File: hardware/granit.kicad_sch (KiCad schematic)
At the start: 8 parts

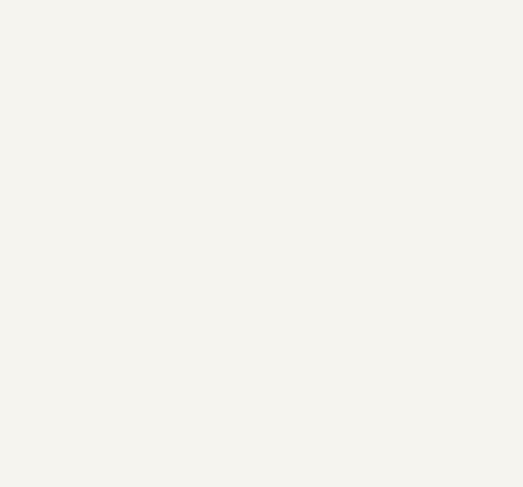
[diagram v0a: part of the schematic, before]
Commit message: feat: add OSHW logo (SYM1) to schematic and PCB
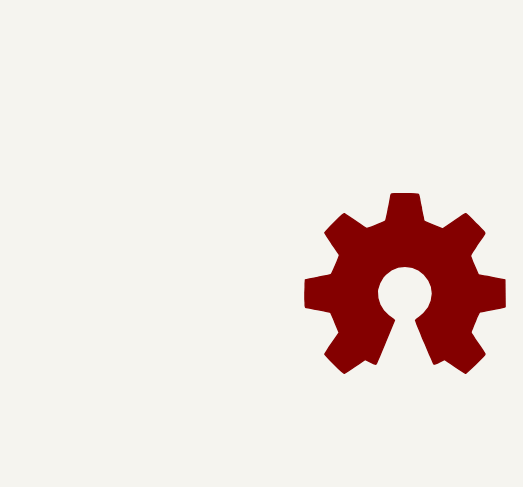
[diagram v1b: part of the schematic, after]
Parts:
- added SYM1: Logo_Open_Hardware_Large, Symbol:OSHW-Logo2_7.3x6mm_SilkScreen, symbol Graphic:Logo_Open_Hardware_Large
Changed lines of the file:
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@@
+	)
+	(symbol
+		(lib_id "Graphic:Logo_Open_Hardware_Large")
+		(at 252.73 143.51 0)
+		(unit 1)
+		(body_style 1)
+		(exclude_from_sim yes)
+		(in_bom no)
+		(on_board yes)
+		(in_pos_files yes)
+		(dnp no)
+		(fields_autoplaced yes)
+		(property "Reference" "SYM1"
+			(at 252.73 130.81 0)
+			(hide yes)
+			(show_name no)
+			(do_not_autoplace no)
+			(effects
+				(font
+					(size 1.27 1.27)
+				)
+			)
+		)
+		(property "Value" "Logo_Open_Hardware_Large"
+			(at 252.73 153.67 0)
+			(hide yes)
+			(show_name no)
+			(do_not_autoplace no)
+			(effects
+				(font
+					(size 1.27 1.27)
+				)
+			)
+		)
+		(property "Footprint" "Symbol:OSHW-Logo2_7.3x6mm_SilkScreen"
+			(at 252.73 143.51 0)
+			(hide yes)
+			(show_name no)
+			(do_not_autoplace no)
+			(effects
+				(font
+					(size 1.27 1.27)
+				)
+			)
+		)
+		(property "Datasheet" ""
+			(at 252.73 143.51 0)
+			(hide yes)
+			(show_name no)
+			(do_not_autoplace no)
+			(effects
+				(font
+					(size 1.27 1.27)
+				)
+			)
+		)
+		(property "Description" "Open Hardware logo, large"
+			(at 252.73 143.51 0)
+			(hide yes)
+			(show_name no)
+			(do_not_autoplace no)
+			(effects
+				(font
+					(size 1.27 1.27)
+				)
+			)
+		)
+		(instances
+			(project "granit"
+				(path "/d2c135e3-a983-4cd4-8cff-b50ca3c7671a"
+					(reference "SYM1")
+					(unit 1)
+				)
+			)
+		)
 	)
 	(symbol
